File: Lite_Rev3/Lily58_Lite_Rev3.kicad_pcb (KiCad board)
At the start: 2 copper layers, 218.5 x 159.5 mm, 118 parts, among them J1 M2HOLE, J10 M2HOLE, J11 M2HOLE, J12 HOLE, J13 HOLE, J14 HOLE, J15 HOLE, J16 OLED_R, J17 breakaway, J18 breakaway, J19 breakaway, J2 M2HOLE, J20 breakaway, J21 breakaway, J22 AudioJack4, J23 HOLE, J24 HOLE, J25 breakaway, J26 breakaway, J3 HOLE, J4 HOLE, J5 HOLE, J6 HOLE, J7 OLED_L, J8 breakaway, J9 AudioJack4, SW1 SW_Push, SW10 SW_Push, SW11 SW_Push, SW12 SW_Push, SW13 SW_Push, SW14 SW_Push, SW15 SW_Push, SW16 SW_Push, SW17 SW_Push, SW18 SW_Push, SW19 SW_Push, SW2 SW_Push, SW20 SW_Push, SW21 SW_Push, SW22 SW_Push, SW23 SW_Push, SW24 SW_Push, SW25 SW_Push, SW26 SW_Push, SW27 SW_Push, SW28 SW_Push, SW29 SW_Push, SW3 SW_Push, SW30 SW_Push, SW31 SW_Push, SW32 SW_Push, SW33 SW_Push, SW34 SW_Push, SW35 SW_Push, SW36 SW_Push, SW37 SW_Push, SW38 SW_Push, SW39 SW_Push, SW4 SW_Push, SW40 SW_Push, SW41 SW_Push, SW42 SW_Push, SW43 SW_Push, SW44 SW_Push, SW45 SW_Push, SW46 SW_Push, SW47 SW_Push, SW48 SW_Push, SW49 SW_Push, SW5 SW_Push, SW50 SW_Push, SW51 SW_Push, SW52 SW_Push, SW53 SW_Push, SW54 SW_Push, SW55 SW_Push, SW56 SW_Push, SW57 SW_Push, SW58 SW_Push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

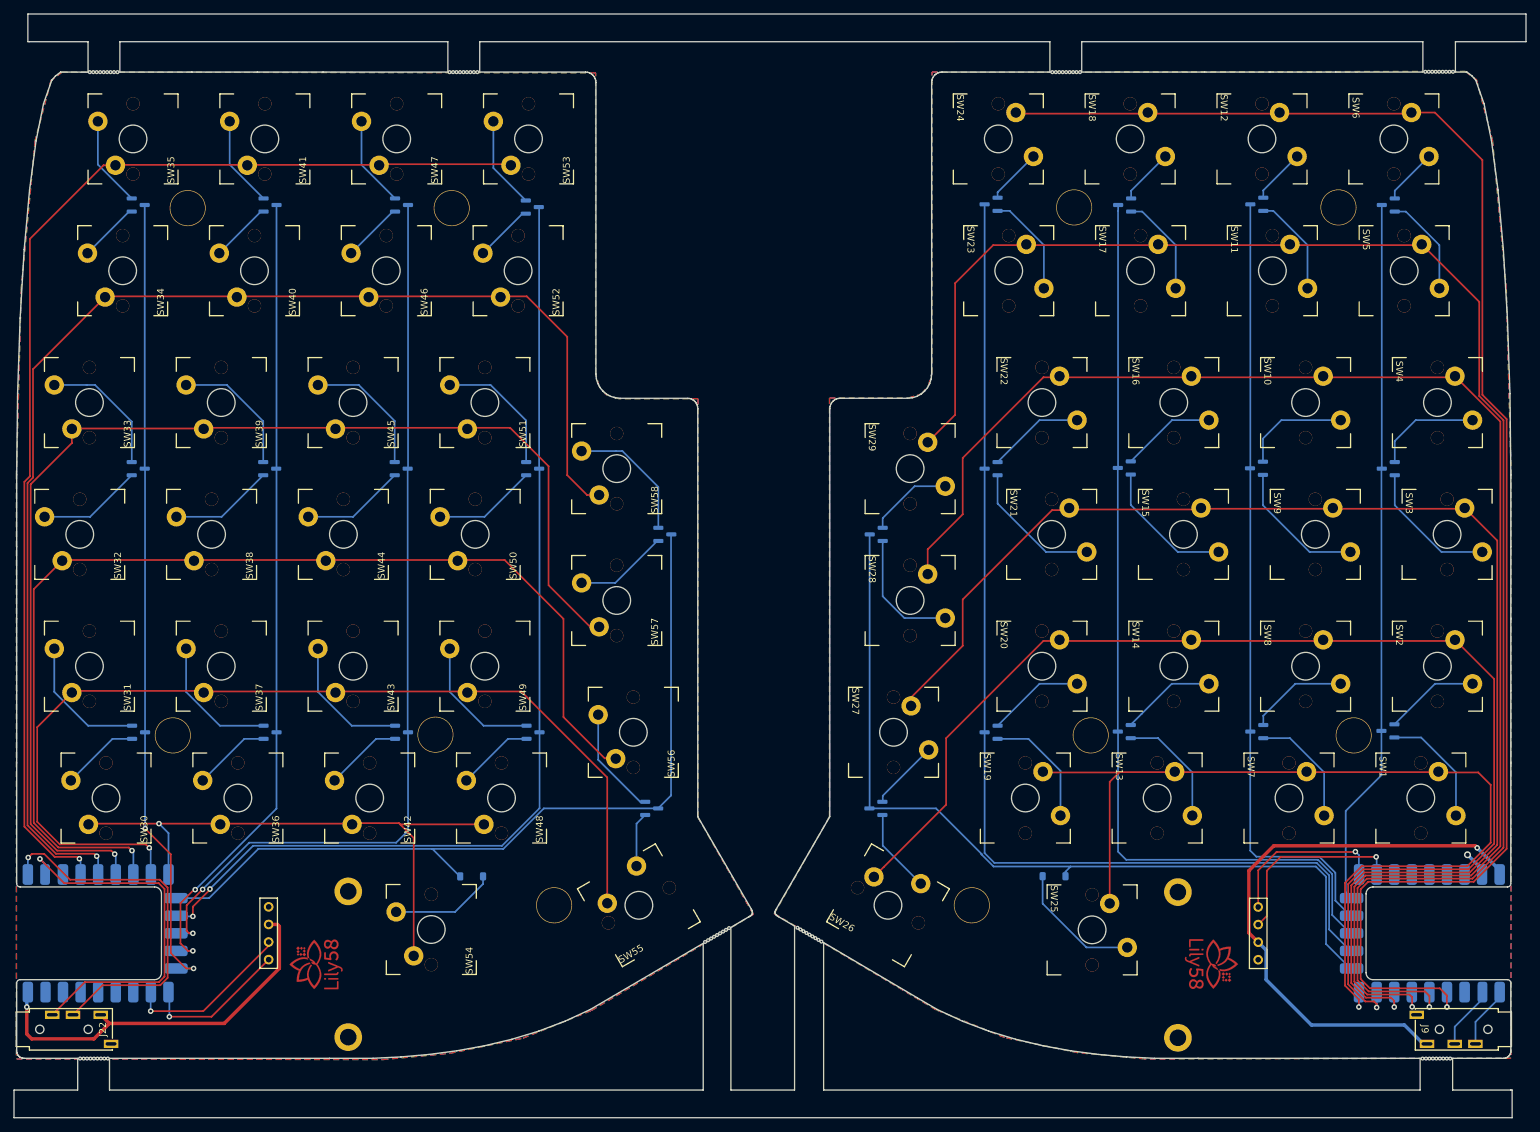
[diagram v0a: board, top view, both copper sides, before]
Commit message: [Lily58 Lite Rev3] Fix SW54
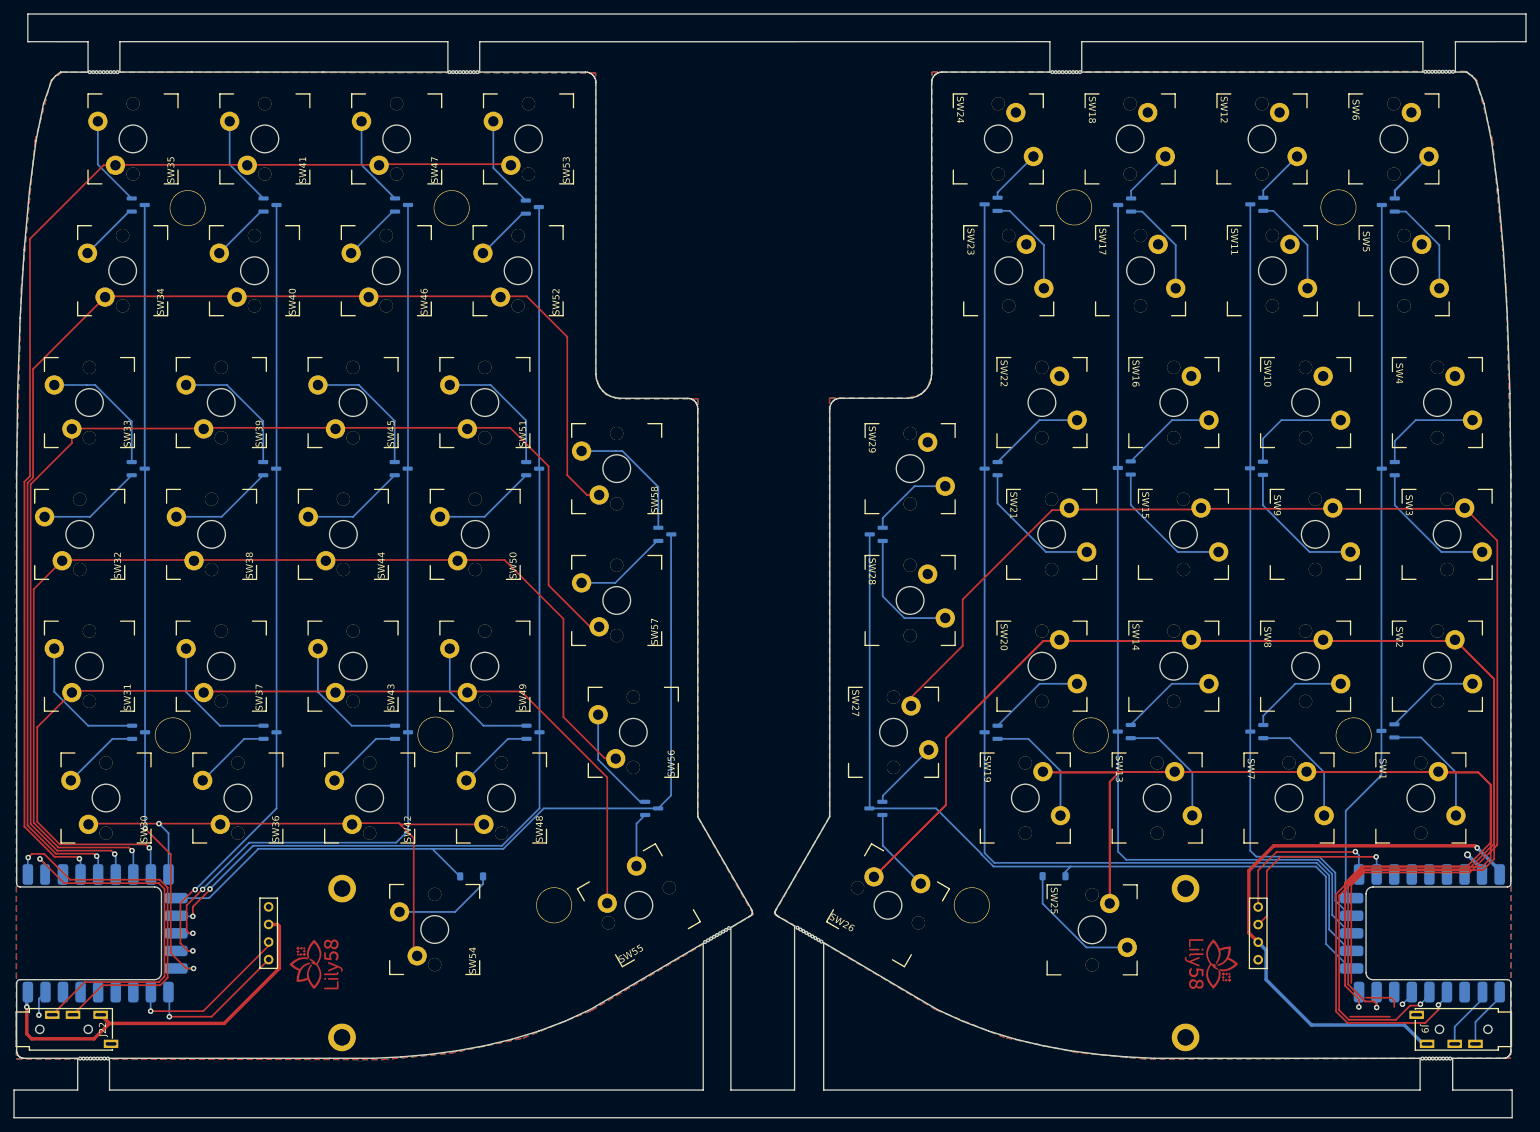
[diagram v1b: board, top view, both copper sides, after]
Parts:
- moved J10 1.22 mm to (273.7, 177.3)
- moved J11 1.11 mm to (273.7, 198.8)
- moved J2 0.96 mm to (151.8, 177.3)
- moved J1 0.90 mm to (151.8, 198.8)
- moved SW54 0.50 mm to (165.2, 183.2)
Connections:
- U1 pad 2: LED_L_LV -> unconnected-(U1-GP2-Pad2)
- U2 pad 2: LED_R -> unconnected-(U2-GP2-Pad2)
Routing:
- net ROW3_L: track 157.2 -> 18.8 mm
- net Net-(D10-A-Pad1): track 14.0 -> 148.0 mm, vias 0 -> 2
- net ROW3_R: track 148.0 -> 14.7 mm, vias 2 -> 0
- net Net-(D7-A-Pad1): track 13.7 -> 134.1 mm, vias 0 -> 2
- net RX: track 9.14 -> 126.3 mm
- net Net-(D15-A): track 18.8 -> 135.6 mm
- net COL5_R: track 171.6 -> 57.0 mm
- net ROW2_R: track 134.1 -> 19.8 mm, vias 2 -> 0
- net Net-(D13-A-Pad1): track 10.3 -> 121.1 mm
- net ROW1_R: track 117.3 -> 9.41 mm, vias 2 -> 0
- net ROW4_R: track 121.1 -> 15.0 mm
- net Net-(D4-A-Pad1): track 14.4 -> 117.3 mm, vias 0 -> 2
- net ROW0_L: track 102.7 -> 18.3 mm
- net COL5_L: track 225.4 -> 156.7 mm
- net COL0_R: track 85.4 -> 143.7 mm
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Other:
- board text added: "2024-10-15"
- board text added: "Lily58 Lite Rev3 v6"
- board text added: "PCB Design by yuchi(Liliums)"
- board text added: "PCB-R"
- board text removed: "2024-07-18"
- board text removed: "Lily58 Lite Rev3 v3 PCBA"

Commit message: [Lily58 Lite Rev3] fix PCB
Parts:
- moved J10 1.22 mm to (272.6, 177.8)
- moved J11 1.11 mm to (272.6, 198.8)
- moved J2 0.96 mm to (152.7, 177.7)
- moved J1 0.90 mm to (152.7, 198.8)
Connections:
- U1 pad 2: unconnected-(U1-GP2-Pad2) -> LED_L_LV
- U2 pad 2: unconnected-(U2-GP2-Pad2) -> LED_R
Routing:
- net ROW3_L: track 18.8 -> 157.2 mm
- net Net-(D10-A-Pad1): track 148.0 -> 14.0 mm, vias 2 -> 0
- net ROW3_R: track 14.7 -> 148.0 mm, vias 0 -> 2
- net Net-(D7-A-Pad1): track 134.1 -> 13.7 mm, vias 2 -> 0
- net RX: track 126.3 -> 9.14 mm
- net Net-(D15-A): track 135.6 -> 18.8 mm
- net COL5_R: track 57.0 -> 171.6 mm
- net ROW2_R: track 19.8 -> 134.1 mm, vias 0 -> 2
- net Net-(D13-A-Pad1): track 121.1 -> 10.3 mm
- net ROW1_R: track 9.41 -> 117.3 mm, vias 0 -> 2
- net ROW4_R: track 15.0 -> 121.1 mm
- net Net-(D4-A-Pad1): track 117.3 -> 14.4 mm, vias 2 -> 0
- net ROW0_L: track 18.3 -> 102.7 mm
- net COL5_L: track 156.7 -> 225.4 mm
- net COL0_R: track 143.7 -> 85.6 mm
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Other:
- board text added: "Lily58 Lite Rev3 v3 PCBA"
- board text removed: "Lily58 Lite Rev3 v6"
- board text removed: "PCB Design by yuchi(Liliums)"
- board text removed: "PCB-R"
